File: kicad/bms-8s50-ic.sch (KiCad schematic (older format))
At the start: 21 parts, among them J1 Conn_01x10, J2 UEXT, J3 USB_B_Micro, P1 CONN_01X01, P2 CONN_01X01, P3 CONN_01X01, P4 CONN_01X01

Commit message: Fix issues found during testing (v0.1.1)
- Add BAT+/- and EXT+/- markings to terminals (#2)
- Change C30 to 470nF (#5)
- Add C20 (47nF) at VC0 pin (#5)
- Add C21 and R72 for proper low-pass filter of VDD (#5)
- Change C39 at VREF to 1uF (#5)
- Add R70: Pull-down for PCHG FET (#5)
- Add R73: Weak pull-down for 5V supply (#6)
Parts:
- added R73: 330k, LibreSolar:R_0603_1608, symbol Project:R
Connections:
- net +5V: now also R73.1
- net GND: now also R73.2
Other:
- note added: "Libre Solar BMS for 3-8 cells"
- note added: "Plug: Würth WR-MPC3\nPart-no. 662014113322\nUse low force crimp contacts!"
- note removed: "Plug part no. \n662014113322"
- moved on the sheet: H1, H2, J1, J2, J3, JP1, JP2, P1, P2, P3, P4, R27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

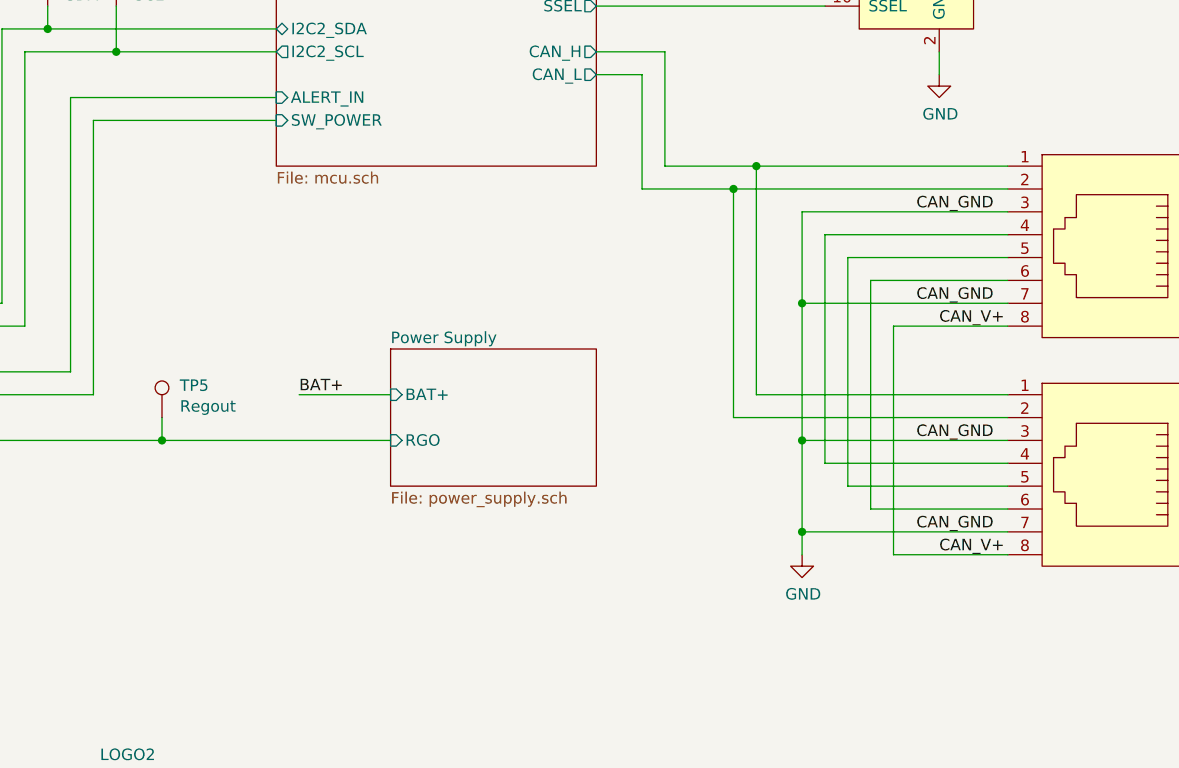
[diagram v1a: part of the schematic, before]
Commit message: Update to v0.2
- Switch to STM32L452 MCU (STM32F072 has too little RAM for CAN ISO-TP etc.)
- Add CAN termination jumper
- Add CAN bus power supply diodes
- Update CAN connector to match LS.bus spec
- Add interactive BOM and CSV BOM to build directory
- Add additional thermal vias with 0.2mm diameter under MOSFETs
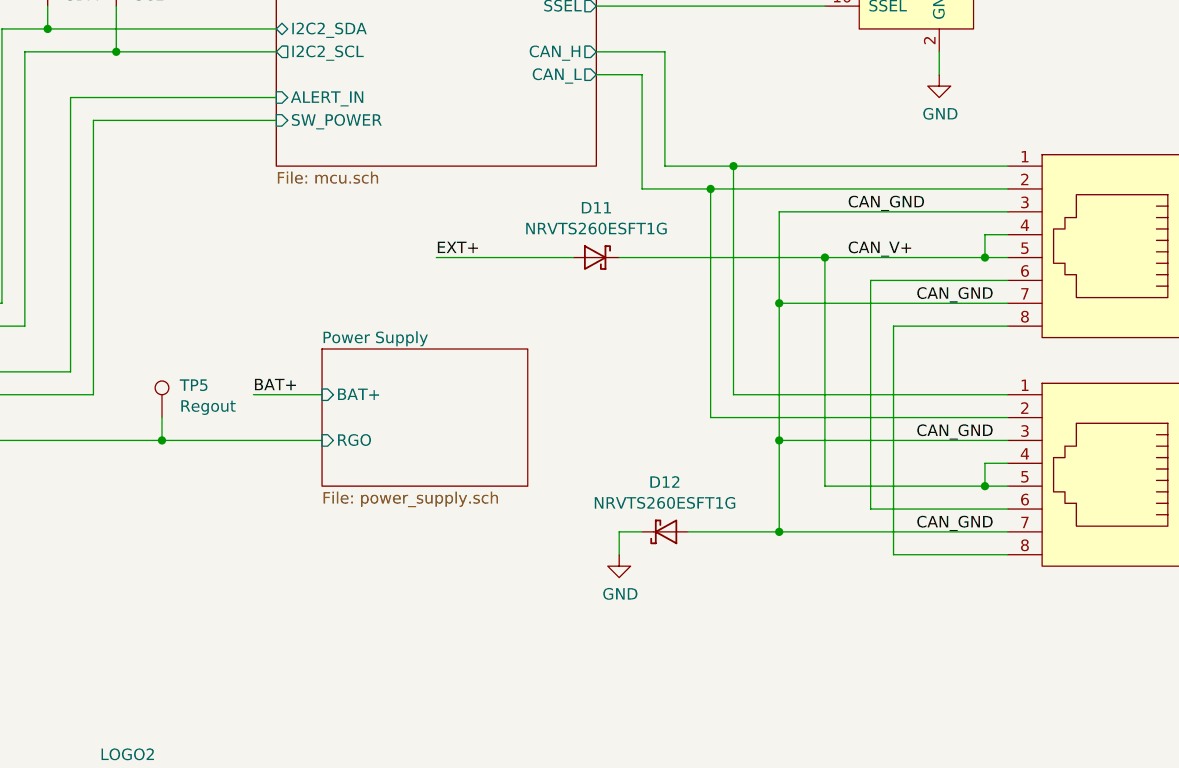
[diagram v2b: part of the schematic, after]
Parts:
- added D11, D12: NRVTS260ESFT1G, Diode_SMD:D_SOD-123, symbol LibreSolar:D_Schottky
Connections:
- net CAN_V+: now also JP1.4, JP1.5, JP2.4, JP2.5, D11.1 (K); no longer JP1.8, JP2.8
- net EXT+: now also D11.2 (A)
- net GND: now also D12.1 (K); no longer JP1.3, JP1.7, JP2.3, JP2.7
- new net: JP1.8, JP2.8
- new net CAN_GND: D12.2 (A), JP1.3, JP1.7, JP2.3, JP2.7
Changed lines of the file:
@@
 Sheet 1 5
 Title "BMS 8S50 IC"
-Date "2020-05-08"
-Rev "0.1.1"
-Comp "Libre Solar"
-Comment1 "License: CC-BY-SA"
+Date "2021-02-13"
+Rev "0.2"
+Comp "Libre Solar Technologies GmbH"
+Comment1 "Website: https://libre.solar"
 Comment2 "Author: Martin Jäger"
-Comment3 ""
+Comment3 "License: Creative Commons Attribution-ShareAlike 4.0 International"
 Comment4 ""
 $EndDescr
 $Sheet
-S 6800 5000 900  600
+S 6500 5000 900  600
 U 58363B12
 F0 "Power Supply" 50
 F1 "power_supply.sch" 50
-F2 "RGO" I L 6800 5400 50
-F3 "BAT+" I L 6800 5200 50
+F2 "RGO" I L 6500 5400 50
+F3 "BAT+" I L 6500 5200 50
 $EndSheet
 $Comp
@@
 	0    1    1    0
 $EndComp
-Text Label 9200 5900 0    50   ~ 0
-CAN_V+
 Text Label 9100 5800 0    50   ~ 0
 CAN_GND
-Text Label 9100 5400 0    50   ~ 0
-CAN_GND
-Text Label 9200 4900 0    50   ~ 0
+Text Label 8800 4600 0    50   ~ 0
 CAN_V+
 Text Label 9100 4800 0    50   ~ 0
 CAN_GND
-Text Label 9100 4400 0    50   ~ 0
+Text Label 8800 4400 0    50   ~ 0
 CAN_GND
 Wire Wire Line
-	8400 5200 9500 5200
-Wire Wire Line
-	8300 5300 9500 5300
-Wire Wire Line
-	8600 4400 8600 4800
-Wire Wire Line
-	8600 4400 9500 4400
-Wire Wire Line
-	8600 4800 9500 4800
-Wire Wire Line
-	8600 4800 8600 5400
-Wire Wire Line
-	8600 5400 9500 5400
-Connection ~ 8600 4800
-Wire Wire Line
-	8600 5400 8600 5800
-Wire Wire Line
-	8600 5800 9500 5800
-Connection ~ 8600 5400
+	8300 5200 9500 5200
+Wire Wire Line
+	8200 5300 9500 5300
+Wire Wire Line
+	8500 4400 8500 4800
+Wire Wire Line
+	8500 4400 9500 4400
+Wire Wire Line
+	8500 4800 9500 4800
+Wire Wire Line
+	8500 4800 8500 5400
+Connection ~ 8500 4800
+Wire Wire Line
+	8500 5400 8500 5800
+Wire Wire Line
+	8500 5800 9500 5800
+Connection ~ 8500 5400
 $Comp
 L power:GND #PWR0120
 U 1 1 5CCBF1D5
-P 8600 5900
-F 0 "#PWR0120" H 8600 5650 50  0001 C CNN
-F 1 "GND" H 8605 5727 50  0000 C CNN
-F 2 "" H 8600 5900 50  0001 C CNN
-F 3 "" H 8600 5900 50  0001 C CNN
-	1    8600 5900
-	1    0    0    -1
-$EndComp
-Wire Wire Line
-	8600 5800 8600 5900
-Connection ~ 8600 5800
-Wire Wire Line
-	9500 4500 8700 4500
-Wire Wire Line
-	8700 4500 8700 5500
-Wire Wire Line
-	8700 5500 9500 5500
+P 7800 5900
+F 0 "#PWR0120" H 7800 5650 50  0001 C CNN
+F 1 "GND" H 7805 5727 50  0000 C CNN
+F 2 "" H 7800 5900 50  0001 C CNN
+F 3 "" H 7800 5900 50  0001 C CNN
+	1    7800 5900
+	1    0    0    -1
+$EndComp
+Wire Wire Line
+	9500 4500 9400 4500
 $Sheet
 S 6300 2000 1400 2200
@@
 	7700 3700 8000 3700
 Wire Wire Line
-	8400 4200 9500 4200
+	8300 4200 9500 4200
 Wire Wire Line
 	7700 3800 7900 3800
 Wire Wire Line
-	8300 4300 9500 4300
-Wire Wire Line
-	8400 4200 8400 5200
-Wire Wire Line
-	8300 4300 8300 5300
+	8200 4300 9500 4300
+Wire Wire Line
+	8300 4200 8300 5200
+Wire Wire Line
+	8200 4300 8200 5300
 Wire Wire Line
 	8000 3700 8000 4200
 Wire Wire Line
-	8000 4200 8400 4200
-Connection ~ 8400 4200
-Wire Wire Line
-	8300 4300 7900 4300
+	8000 4200 8300 4200
+Connection ~ 8300 4200
+Wire Wire Line
+	8200 4300 7900 4300
 Wire Wire Line
 	7900 4300 7900 3800
-Connection ~ 8300 4300
+Connection ~ 8200 4300
 Wire Wire Line
 	2400 4300 2800 4300
@@
 Wire Wire Line
 	4800 1900 4800 4600
-Text Label 6400 5200 0    50   ~ 0
+Text Label 6200 5200 0    50   ~ 0
 BAT+
 Wire Wire Line
@@
 Connection ~ 5800 5400
 Wire Wire Line
-	5800 5400 6800 5400
+	5800 5400 6500 5400
 Wire Wire Line
 	9000 4900 9000 5900
@@
 	8900 4700 9500 4700
 Wire Wire Line
-	9500 4600 8800 4600
+	9500 4600 9400 4600
 Wire Wire Line
 	8900 4700 8900 5700
 Wire Wire Line
-	8800 4600 8800 5600
-Wire Wire Line
-	8800 5600 9500 5600
+	8700 5600 9400 5600
 Wire Wire Line
 	4100 2000 4700 2000
@@
 Text Label 5000 1900 0    50   ~ 0
 EXT+
-Wire Wire Line
-	6400 5200 6800 5200
 Text Notes 1500 6200 0    50   ~ 0
 Plug: Würth WR-MPC3\nPart-no. 662014113322\nUse low force crimp contacts!
@@
 Text Notes 1900 1100 0    200  ~ 0
 Libre Solar BMS for 3-8 cells
+Text Label 9100 5400 0    50   ~ 0
+CAN_GND
+Wire Wire Line
+	8500 5400 9500 5400
+Wire Wire Line
+	9400 4500 9400 4600
+Wire Wire Line
+	9400 5500 9400 5600
+Wire Wire Line
+	9400 5500 9500 5500
+Connection ~ 9400 5600
+Wire Wire Line
+	9400 5600 9500 5600
+Wire Wire Line
+	9400 4600 8700 4600
+Wire Wire Line
+	8700 4600 8700 5600
+Connection ~ 9400 4600
+Text Label 7000 4600 0    50   ~ 0
+EXT+
+$Comp
+L LibreSolar:D_Schottky D11
+U 1 1 604A441C
+P 7700 4600
+F 0 "D11" H 7700 4384 50  0000 C CNN
+F 1 "NRVTS260ESFT1G" H 7700 4475 50  0000 C CNN
+F 2 "Diode_SMD:D_SOD-123" H 7600 4600 50  0001 C CNN
+F 3 "" H 7700 4700 50  0001 C CNN
+F 4 "On Semiconductor" H 7700 4600 50  0001 C CNN "Manufacturer"
+F 5 "NRVTS260ESFT1G" H 7700 4600 50  0001 C CNN "PartNumber"
+F 6 "Alternative: Nexperia PMEG6020ER,115" H 7700 4600 50  0001 C CNN "Remarks"
+	1    7700 4600
+	-1   0    0    1
+$EndComp
+Wire Wire Line
+	8700 4600 7800 4600
+Connection ~ 8700 4600
+Wire Wire Line
+	7600 4600 7000 4600
+$Comp
+L LibreSolar:D_Schottky D12
+U 1 1 604BC955
+P 8000 5800
+F 0 "D12" H 8000 6016 50  0000 C CNN
+F 1 "NRVTS260ESFT1G" H 8000 5925 50  0000 C CNN
+F 2 "Diode_SMD:D_SOD-123" H 7900 5800 50  0001 C CNN
+F 3 "" H 8000 5900 50  0001 C CNN
+F 4 "On Semiconductor" H 8000 5800 50  0001 C CNN "Manufacturer"
+F 5 "NRVTS260ESFT1G" H 8000 5800 50  0001 C CNN "PartNumber"
+F 6 "Alternative: Nexperia PMEG6020ER,115" H 8000 5800 50  0001 C CNN "Remarks"
+	1    8000 5800
+	1    0    0    -1
+$EndComp
+Wire Wire Line
+	7800 5800 7800 5900
+Wire Wire Line
+	8500 5800 8100 5800
+Connection ~ 8500 5800
+Wire Wire Line
+	7900 5800 7800 5800
+Wire Wire Line
+	6500 5200 6200 5200
 $EndSCHEMATC
